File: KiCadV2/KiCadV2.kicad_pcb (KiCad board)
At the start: 2 copper layers, 149 parts, among them J1 USB_C_Receptacle_PowerOnly_6P, J2 Screw_Terminal_01x02, J3 Screw_Terminal_01x02, J4 Screw_Terminal_01x02, U1 MT3608, U10 NC7SZ157P6X, U11 NC7SZ157P6X, U12 NC7SZ157P6X, U13 NC7SZ157P6X, U14 74LV08AT14-13, U15 HIP4080A, U16 NC7SZ157P6X, U17 MX3502S, U18 MX3502S, U2 74HC595, U22 DMHT10H032LFJ, U23 INA240A1D, U26 MX3502S, U3 NC7SZ157P6X, U30 DMHT10H032LFJ, U31 INA240A1D, U32 NC7SZ157P6X, U33 NC7SZ157P6X, U34 NC7SZ157P6X, U35 NC7SZ157P6X, U36 NC7SZ157P6X, U37 NC7SZ157P6X, U38 74LV08AT14-13, U39 HIP4080A, U4 NC7SZ157P6X, U40 MCP6002-xSN, U41 CJ432, U5 MX3502S, U6 NC7SZ157P6X, U7 DAC082S085CISDX/NOPB, U8 NC7SZ157P6X, U9 NC7SZ157P6X

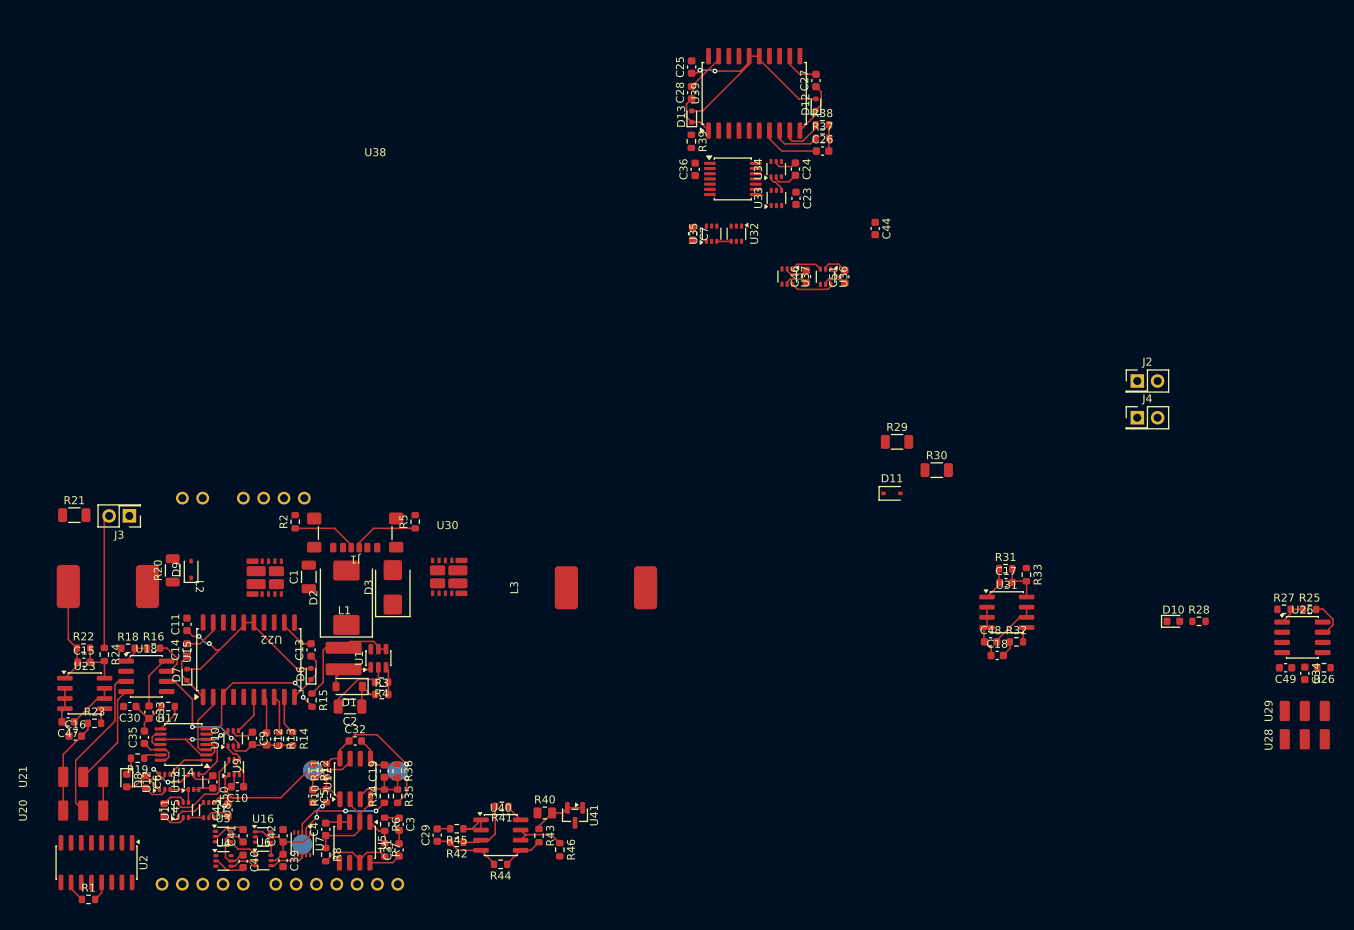
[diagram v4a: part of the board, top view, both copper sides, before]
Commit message: PCB - Right side coil done
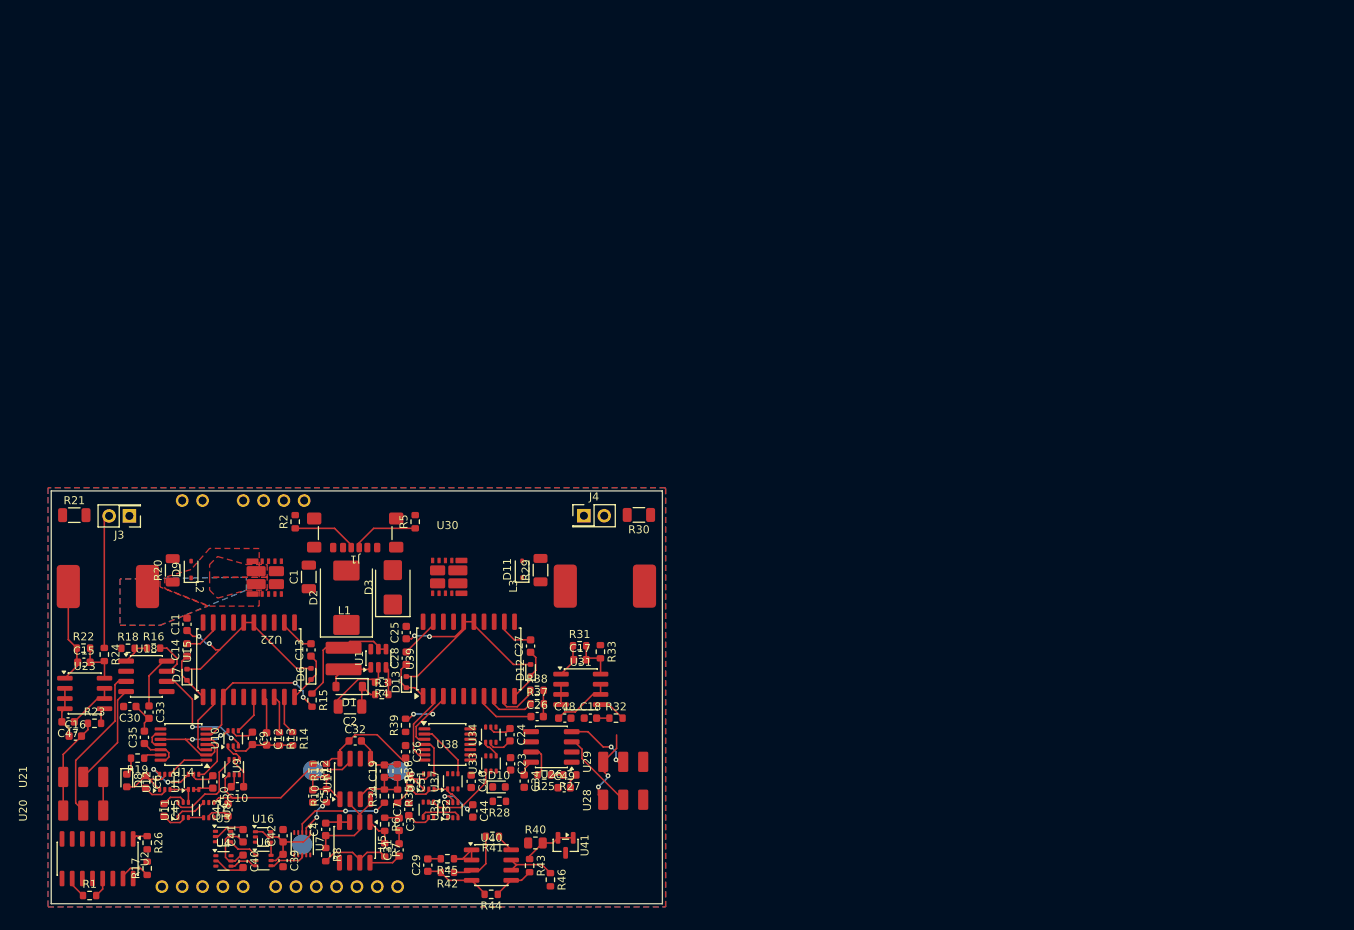
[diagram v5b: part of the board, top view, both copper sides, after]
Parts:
- removed J2: Screw_Terminal_01x02, Connector_PinHeader_2.54mm:PinHeader_2x01_P2.54mm_Vertical
- moved R26 148.7 mm to (69.8, 166.6), turned to -90 degrees
- moved C34 98.5 mm to (116.9, 158.9)
- moved R25 97.9 mm to (119.4, 158.1), turned to 180 degrees
- moved U26 94.9 mm to (120.3, 154.6), turned to 180 degrees
- moved R27 91.6 mm to (122.6, 158.1), turned to 180 degrees
- moved C49 91.4 mm to (121.9, 159.7), turned to 0 degrees
- moved R28 90.3 mm to (113.8, 161.4), turned to 180 degrees
- moved C44 88.5 mm to (110.5, 162.6)
- moved D10 86.8 mm to (113.8, 159.6)
- moved U28 85.5 mm to (122.3, 161.2)
- moved U29 85.4 mm to (122.3, 156.5)
- moved C51 83.3 mm to (102.6, 158.9), turned to -90 degrees
- moved U32 81.6 mm to (105.0, 162.4)
- moved C36 81.3 mm to (102.1, 155.2), turned to -90 degrees
- moved R39 81.3 mm to (102.1, 151.9), turned to 90 degrees
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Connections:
- R25 pad 1: Net-(U26B-+) -> Net-(U26A-+)
- R27 pad 2: Net-(U26B-+) -> Net-(U26A-+)
- U26 pad 2: Net-(U26A--) -> /PerCoil1/OC_SENSE
- U26 pad 4: /PerCoil1/OC_SENSE -> Net-(U26B--)
- U26 pad 6: /PerCoil1/~{OC1} -> /PerCoil1/SignalProcessingChain/Current_Dir
- U26 pad 7: /PerCoil1/SignalProcessingChain/Current_Dir -> /PerCoil1/~{OC1}
- U28 pad 2: Net-(U26A-+) -> Net-(U26B-+)
- U29 pad 2: Net-(U26A--) -> Net-(U26B--)
- U38 pad 1: Net-(U36-Z) -> /PerCoil1/SignalProcessingChain/EN
- U38 pad 2: /PerCoil1/SignalProcessingChain/EN -> Net-(U37-Z)
- U38 pad 3: /PerCoil1/SignalProcessingChain/HEN -> /PerCoil1/SignalProcessingChain/DIS
- U38 pad 4: /PerCoil1/SignalProcessingChain/EN -> Net-(U36-Z)
- U38 pad 5: Net-(U37-Z) -> /PerCoil1/SignalProcessingChain/EN
- U38 pad 6: /PerCoil1/SignalProcessingChain/DIS -> /PerCoil1/SignalProcessingChain/HEN
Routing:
- net /PerCoil1/SignalProcessingChain/DIS: track 0.00 -> 11.7 mm, vias 0 -> 2
- net Net-(U26B-+): track 0.00 -> 10.1 mm
- net /PerCoil1/SignalProcessingChain/HF PWM: track 0.00 -> 9.54 mm
- net +5V: track 106.1 -> 115.6 mm, vias 2 -> 4
- net /A2: track 1.93 -> 11.4 mm, vias 0 -> 2
- net /PerCoil1/SignalProcessingChain/HEN: track 0.00 -> 9.36 mm
- net GND: track 87.0 -> 77.9 mm
- net Net-(U26B--): track 0.00 -> 8.58 mm, vias 0 -> 2
- net Net-(U37-Z): track 0.00 -> 7.25 mm
- net /C2: track 5.49 -> 0.00 mm
- net Net-(U36-Z): track 0.00 -> 4.61 mm
- net Net-(U32-Z): track 1.80 -> 5.27 mm
- net Net-(U26A-+): track 3.69 -> 1.65 mm
- net /0.2V: track 0.18 -> 2.09 mm
- net /EN2: track 0.02 -> 1.90 mm
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- added copper zone on F.Cu, net /+OUT1
- added copper zone on B.Cu, net /PerCoil/BHS
- added copper zone on F.Cu, net /PerCoil/BHS
- added copper zone on F.Cu, net /PerCoil/OC_SENSE
- added copper zone on B.Cu, net GND
- added copper zone on F.Cu, net GND
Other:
- board outline added: 76.4 x 51.6 mm

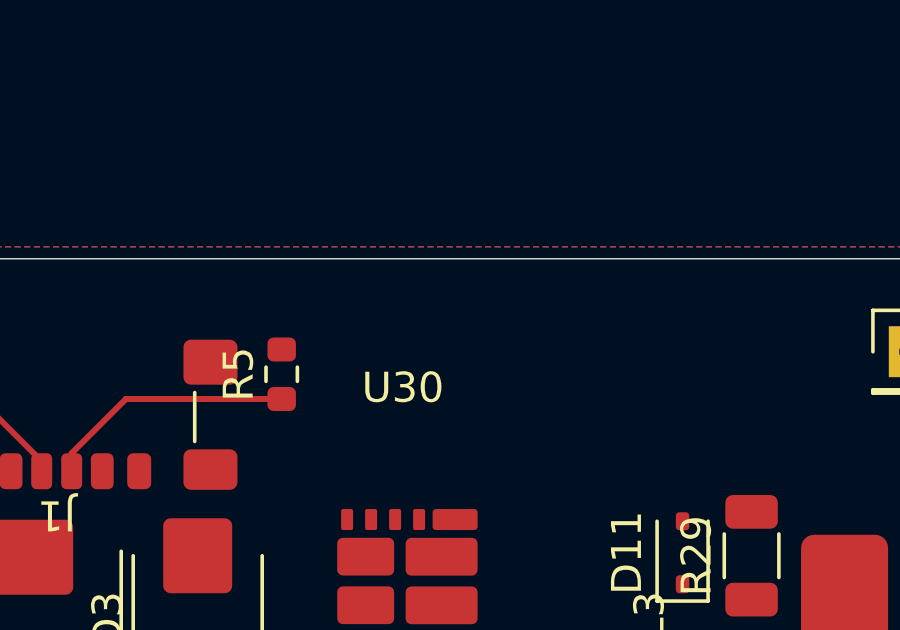
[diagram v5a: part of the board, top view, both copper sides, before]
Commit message: Added LEDs to schematic & PCB
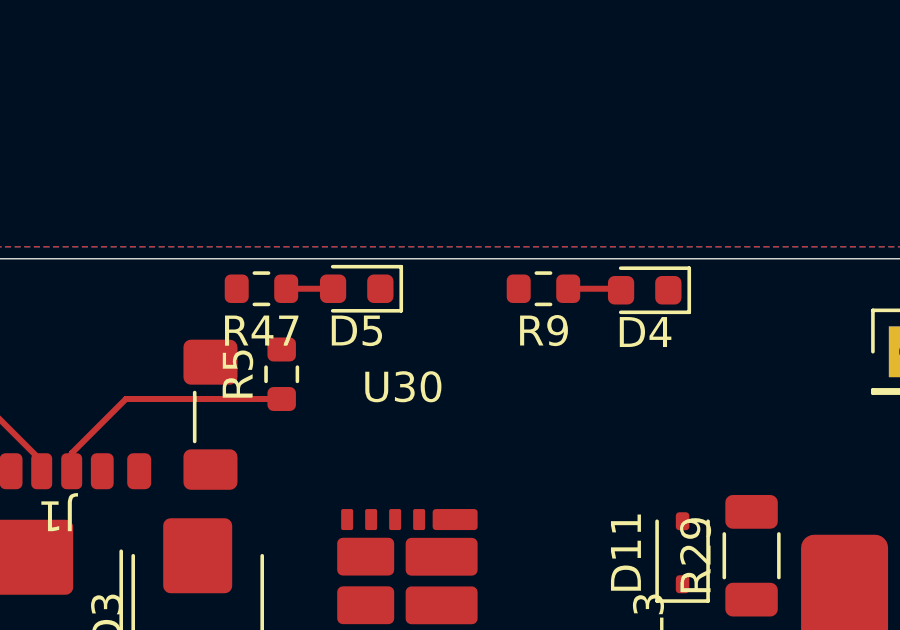
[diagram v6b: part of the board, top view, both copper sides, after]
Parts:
- added D4: KT-0603W, LED_SMD:LED_0603_1608Metric, F.Cu at (115.4, 123.7)
- added D5: KT-0603W, LED_SMD:LED_0603_1608Metric, F.Cu at (105.8, 123.6)
- added R47: 390, Resistor_SMD:R_0603_1608Metric, F.Cu at (102.6, 123.6)
- added R9: 390, Resistor_SMD:R_0603_1608Metric, F.Cu at (112.0, 123.6)
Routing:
- net Net-(D4-A): track 0.00 -> 1.78 mm
- net Net-(D5-A): track 0.00 -> 1.56 mm

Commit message: Update KiCadV2.kicad_pcb
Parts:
- removed U20, U21, U28, U29: ~, TestPoint:SPDT_solder_bridge
- moved J3 2.58 mm to (65.0, 125.7), turned to 0 degrees
- moved C15 2.43 mm to (59.6, 143.2), turned to -90 degrees
- moved R31 1.49 mm to (125.0, 142.9), turned to -90 degrees
- moved C17 1.20 mm to (123.0, 142.9), turned to -90 degrees
- moved R39 1.19 mm to (101.2, 151.1), turned to 0 degrees
- moved R22 0.98 mm to (61.6, 143.2), turned to -90 degrees
- moved R24 0.80 mm to (63.6, 143.0)
- moved R33 0.49 mm to (126.9, 142.9)
- moved U30 0.07 mm to (107.3, 127.5)
- turned R21 to 180 degrees
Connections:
- net Net-(U31--) renamed /SenseR
- A1 pad 10: /A2 -> /Analog2
- A1 pad 9: /A1 -> /Analog1
- C13 pad 2: /+OUT1 -> /PerCoil/AHS
- C14 pad 2: /PerCoil/BHS -> /-OUT1
- C15 pad 1: Net-(U23--) -> /+OUT1
- C16 pad 2: /A1 -> /Analog1
- C18 pad 2: /A2 -> /Analog2
- L2 pad 1: /PerCoil/BHS -> /PerCoil/AHS
- L2 pad 2: Net-(U23--) -> /SenseL
- R21 pad 1: Net-(U23--) -> /+OUT1
- R21 pad 2: /-OUT1 -> /SenseL
- R22 pad 1: Net-(U23--) -> /+OUT1
- R23 pad 1: /A1 -> /Analog1
- R24 pad 1: /-OUT1 -> /SenseL
- R32 pad 1: /A2 -> /Analog2
- U15 pad 12: /+OUT1 -> /PerCoil/AHS
- U15 pad 19: /PerCoil/BHS -> /-OUT1
- U18 pad 3: Net-(U18B-+) -> /Analog1
- U18 pad 4: Net-(U18B--) -> /VCM
- U22 pad 1: /PerCoil/AH -> /PerCoil/BH
- U22 pad 10: /PerCoil/BH -> /PerCoil/AH
- U22 pad 3: /+OUT1 -> /-OUT1
- U22 pad 4: /PerCoil/AL -> /PerCoil/BL
- U22 pad 7: /PerCoil/BL -> /PerCoil/AL
- U22 pad 8: /PerCoil/BHS -> /PerCoil/AHS
- U23 pad 1: Net-(U23--) -> /+OUT1
- U26 pad 3: Net-(U26B-+) -> /Analog2
- U26 pad 4: Net-(U26B--) -> /VCM
- U30 pad 1: /PerCoil1/AH -> /PerCoil1/BH
- U30 pad 10: /PerCoil1/BH -> /PerCoil1/AH
- U30 pad 3: /+OUT2 -> /PerCoil1/BHS
- U30 pad 4: /PerCoil1/AL -> /PerCoil1/BL
- U30 pad 7: /PerCoil1/BL -> /PerCoil1/AL
- U30 pad 8: /PerCoil1/BHS -> /+OUT2
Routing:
- net +12V: track 60.4 -> 112.8 mm, vias 4 -> 9
- net /+OUT1: track 4.66 -> 26.9 mm
- net VBUS: track 14.9 -> 35.4 mm, vias 0 -> 22
- net Net-(U18B-+): track 19.7 -> 0.00 mm
- net /PerCoil1/AH: track 0.00 -> 16.8 mm, vias 0 -> 2
- net /-OUT2: track 0.00 -> 16.4 mm
- net /PerCoil/BH: track 0.00 -> 16.3 mm, vias 0 -> 2
- net /SenseR: track 4.78 -> 18.9 mm
- net Net-(U23--): track 13.6 -> 0.00 mm
- net Net-(U18B--): track 12.9 -> 0.00 mm
- net /PerCoil1/AL: track 0.00 -> 12.2 mm, vias 0 -> 2
- net /A1: track 23.1 -> 10.9 mm
- net /PerCoil/BL: track 0.00 -> 12.0 mm, vias 0 -> 2
- net /A2: track 11.4 -> 0.00 mm, vias 2 -> 0
- net /+OUT2: track 4.82 -> 16.2 mm, vias 0 -> 13
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- added copper zone on F.Cu, net +12V
- added copper zone on B.Cu, net /+OUT2
- added copper zone on F.Cu, net /+OUT2
- added copper zone on B.Cu, net /-OUT1
- added copper zone on F.Cu, net /-OUT1
- added copper zone on F.Cu, net /-OUT2
- added copper zone on B.Cu, net /PerCoil/AHS
- added copper zone on F.Cu, net /PerCoil/AHS
- added copper zone on B.Cu, net /PerCoil1/BHS
- added copper zone on F.Cu, net /PerCoil1/BHS
- added copper zone on F.Cu, net /PerCoil1/OC_SENSE
- added copper zone on F.Cu, net /SenseL
- added copper zone on F.Cu, net /SenseR
- added copper zone on B.Cu, net VBUS
- added copper zone on F.Cu, net VBUS
- added copper zone on F.Cu, net Vdrive
- removed copper zone on B.Cu, net /PerCoil/BHS
- removed copper zone on F.Cu, net /PerCoil/BHS

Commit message: Gonna push before I revert PCB. PCB seems to have gotten fked at some point.
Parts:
- removed C15, C16, C47: 100n, Capacitor_SMD:C_0603_1608Metric
- removed R22: 820, Resistor_SMD:R_0603_1608Metric
- removed R23, R24: 1k, Resistor_SMD:R_0603_1608Metric
- removed U23: INA240A1D, Package_SO:SOIC-8_3.9x4.9mm_P1.27mm
- moved R1 52.5 mm to (115.1, 171.9), turned to 180 degrees
- moved R17 44.8 mm to (114.6, 169.4)
- moved R26 44.8 mm to (114.6, 166.2)
- moved U2 44.7 mm to (108.3, 168.9)
- moved C29 15.5 mm to (105.3, 184.9)
- moved R40 15.5 mm to (118.7, 182.1)
- moved R41 15.5 mm to (113.3, 181.3)
- moved R42 15.5 mm to (107.7, 185.8)
- moved R43 15.5 mm to (118.0, 184.9)
- moved R44 15.5 mm to (113.2, 188.5)
- moved R45 15.5 mm to (107.7, 184.1)
- moved R46 15.5 mm to (120.6, 186.7)
- moved U40 15.5 mm to (113.2, 184.9)
- moved U41 15.5 mm to (122.5, 182.4)
- moved C36 1.40 mm to (102.0, 153.8)
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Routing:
- net /PerCoil1/OC_SENSE: track 8.13 -> 32.3 mm
- net +5V: track 115.6 -> 102.5 mm, vias 4 -> 2
- net /PerCoil1/~{OC1}: track 4.17 -> 16.7 mm
- net /Analog1: track 10.9 -> 0.00 mm
- net /PerCoil/~{OC1}: track 7.98 -> 18.4 mm
- net GND: track 71.2 -> 61.3 mm
- net Net-(U37-Z): track 7.25 -> 0.00 mm
- net /PerCoil1/SignalProcessingChain/Current_Dir: track 0.00 -> 4.92 mm
- net /Analog2: track 6.43 -> 1.60 mm
- net Net-(U36-Z): track 4.61 -> 0.00 mm
- net /EN1: track 4.10 -> 0.00 mm
- net /D1: track 2.46 -> 6.38 mm
- net /PerCoil1/SignalProcessingChain/EN: track 0.32 -> 4.23 mm
- net Net-(U26A-+): track 1.65 -> 3.82 mm
- net Net-(R23-Pad2): track 2.00 -> 0.00 mm
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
